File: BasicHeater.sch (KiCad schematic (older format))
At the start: 9 parts, among them J13 Thermistor

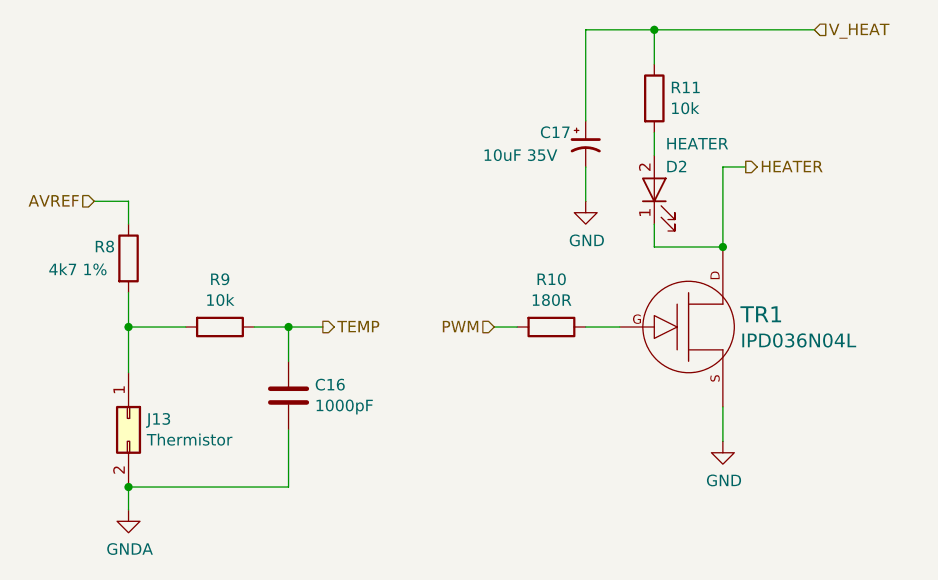
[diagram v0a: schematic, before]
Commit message: Assigned footprints for all components. Inductors are approximate size. MOSFETs dont agree with the footprints. Saved pcb netlist report as report.txt.
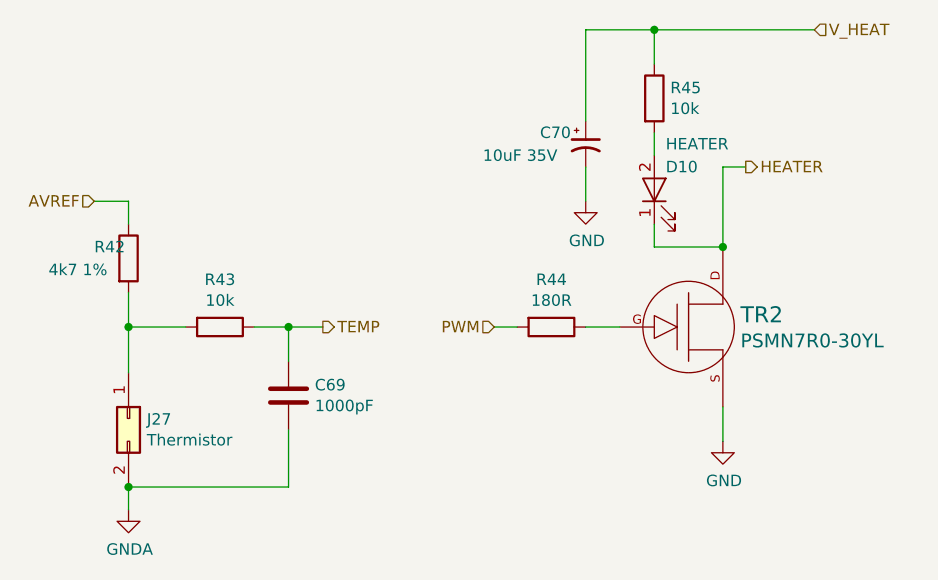
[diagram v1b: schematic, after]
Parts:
- C16: footprint (none) -> Capacitor_SMD:C_0603_1608Metric
- C17: footprint (none) -> Capacitor_SMD:CP_Elec_4x5.3
- D2: footprint (none) -> LED_SMD:LED_0603_1608Metric
- J13: footprint (none) -> Connector_PinHeader_2.54mm:PinHeader_1x02_P2.54mm_Vertical
- R10, R11, R8, R9: footprint (none) -> Resistor_SMD:R_0603_1608Metric
- TR1: value IPD036N04L -> PSMN7R0-30YL; footprint (none) -> Package_TO_SOT_SMD:SOT-669_LFPAK
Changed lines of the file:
@@
 AR Path="/5AC337B6/5AD9F95A/5AD4D269/5AD4D3D5" Ref="J27"  Part="1"
 AR Path="/5AB8F10D/5AD4D3D5" Ref="J28"  Part="1"
-F 0 "J13" V 2954 3730 50  0000 L CNN
+F 0 "J27" V 2954 3730 50  0000 L CNN
 F 1 "Thermistor" V 3045 3730 50  0000 L CNN
-F 2 "" H 2950 3650 50  0001 C CNN
+F 2 "Connector_PinHeader_2.54mm:PinHeader_1x02_P2.54mm_Vertical" H 2950 3650 50  0001 C CNN
 F 3 "~" H 2950 3650 50  0001 C CNN
 	1    2950 3650
@@
 AR Path="/5AC337B6/5AD9F95A/5AD4D269/5AD4D4AD" Ref="R42"  Part="1"
 AR Path="/5AB8F10D/5AD4D4AD" Ref="R46"  Part="1"
-F 0 "R8" H 2800 3000 50  0000 L CNN
+F 0 "R42" H 2800 3000 50  0000 L CNN
 F 1 "4k7 1%" H 2600 2900 50  0000 L CNN
-F 2 "" V 2880 2950 50  0001 C CNN
+F 2 "Resistor_SMD:R_0603_1608Metric" V 2880 2950 50  0001 C CNN
 F 3 "~" H 2950 2950 50  0001 C CNN
 	1    2950 2950
@@
 AR Path="/5AC337B6/5AD9F95A/5AD4D269/5AD4D50F" Ref="R43"  Part="1"
 AR Path="/5AB8F10D/5AD4D50F" Ref="R47"  Part="1"
-F 0 "R9" V 3143 3250 50  0000 C CNN
+F 0 "R43" V 3143 3250 50  0000 C CNN
 F 1 "10k" V 3234 3250 50  0000 C CNN
-F 2 "" V 3280 3250 50  0001 C CNN
+F 2 "Resistor_SMD:R_0603_1608Metric" V 3280 3250 50  0001 C CNN
 F 3 "~" H 3350 3250 50  0001 C CNN
 	1    3350 3250
@@
 AR Path="/5AC337B6/5AD9F95A/5AD4D269/5AD4D569" Ref="C69"  Part="1"
 AR Path="/5AB8F10D/5AD4D569" Ref="C71"  Part="1"
-F 0 "C16" H 3765 3596 50  0000 L CNN
+F 0 "C69" H 3765 3596 50  0000 L CNN
 F 1 "1000pF" H 3765 3505 50  0000 L CNN
-F 2 "" H 3688 3400 50  0001 C CNN
+F 2 "Capacitor_SMD:C_0603_1608Metric" H 3688 3400 50  0001 C CNN
 F 3 "~" H 3650 3550 50  0001 C CNN
 	1    3650 3550
@@
 AR Path="/5AC337B6/5AD9F95A/5AD4D269/5AD4D990" Ref="R44"  Part="1"
 AR Path="/5AB8F10D/5AD4D990" Ref="R48"  Part="1"
-F 0 "R10" V 4593 3250 50  0000 C CNN
+F 0 "R44" V 4593 3250 50  0000 C CNN
 F 1 "180R" V 4684 3250 50  0000 C CNN
-F 2 "" V 4730 3250 50  0001 C CNN
+F 2 "Resistor_SMD:R_0603_1608Metric" V 4730 3250 50  0001 C CNN
 F 3 "~" H 4800 3250 50  0001 C CNN
 	1    4800 3250
@@
 AR Path="/5AC337B6/5AD9F95A/5AD4D269/5AD51003" Ref="TR2"  Part="1"
 AR Path="/5AB8F10D/5AD51003" Ref="TR3"  Part="1"
-F 0 "TR1" H 5627 3303 70  0000 L CNN
-F 1 "IPD036N04L" H 5627 3189 60  0000 L CNN
-F 2 "" H 5400 3250 60  0000 C CNN
+F 0 "TR2" H 5627 3303 70  0000 L CNN
+F 1 "PSMN7R0-30YL" H 5627 3189 60  0000 L CNN
+F 2 "Package_TO_SOT_SMD:SOT-669_LFPAK" H 5400 3250 60  0001 C CNN
 F 3 "" H 5400 3250 60  0000 C CNN
 	1    5400 3250
@@
 AR Path="/5AC337B6/5AD9F95A/5AD4D269/5AD51206" Ref="C70"  Part="1"
 AR Path="/5AB8F10D/5AD51206" Ref="C72"  Part="1"
-F 0 "C17" H 4750 2500 50  0000 L CNN
+F 0 "C70" H 4750 2500 50  0000 L CNN
 F 1 "10uF 35V" H 4500 2400 50  0000 L CNN
-F 2 "" H 4950 2450 50  0001 C CNN
+F 2 "Capacitor_SMD:CP_Elec_4x5.3" H 4950 2450 50  0001 C CNN
 F 3 "~" H 4950 2450 50  0001 C CNN
 	1    4950 2450
@@
 AR Path="/5AC337B6/5AD9F95A/5AD4D269/5AD512CE" Ref="R45"  Part="1"
 AR Path="/5AB8F10D/5AD512CE" Ref="R49"  Part="1"
-F 0 "R11" H 5320 2296 50  0000 L CNN
+F 0 "R45" H 5320 2296 50  0000 L CNN
 F 1 "10k" H 5320 2205 50  0000 L CNN
-F 2 "" V 5180 2250 50  0001 C CNN
+F 2 "Resistor_SMD:R_0603_1608Metric" V 5180 2250 50  0001 C CNN
 F 3 "~" H 5250 2250 50  0001 C CNN
 	1    5250 2250
@@
 AR Path="/5AC337B6/5AD9F95A/5AD4D269/5AD513CB" Ref="D10"  Part="1"
 AR Path="/5AB8F10D/5AD513CB" Ref="D11"  Part="1"
-F 0 "D2" V 5350 2600 50  0000 R CNN
+F 0 "D10" V 5350 2600 50  0000 R CNN
 F 1 "HEATER" V 5450 2600 50  0000 R CNN
-F 2 "" H 5250 2650 50  0001 C CNN
+F 2 "LED_SMD:LED_0603_1608Metric" H 5250 2650 50  0001 C CNN
 F 3 "~" H 5250 2650 50  0001 C CNN
 	1    5250 2650

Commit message: Updated components. Removed power supply. Component layout on PCB.
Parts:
- TR1: footprint Package_TO_SOT_SMD:SOT-669_LFPAK -> PrntrBoardV1:SOT-669_LFPAK
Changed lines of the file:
@@
 $Descr A4 11693 8268
 encoding utf-8
-Sheet 7 35
+Sheet 7 34
 Title ""
 Date ""
@@
 $Comp
 L Connector_Generic:Conn_02x01 J13
-U 1 1 5AD4D3D5
+U 1 1 5ACEEAAB
 P 2950 3650
-AR Path="/5AC337B6/5ACBE919/5AD4D269/5AD4D3D5" Ref="J13"  Part="1"
-AR Path="/5AC337B6/5AD9F95A/5AD4D269/5AD4D3D5" Ref="J27"  Part="1"
-AR Path="/5AB8F10D/5AD4D3D5" Ref="J28"  Part="1"
+AR Path="/5AC337B6/5ACBE919/5AD4D269/5ACEEAAB" Ref="J13"  Part="1"
+AR Path="/5AC337B6/5AD9F95A/5AD4D269/5ACEEAAB" Ref="J27"  Part="1"
+AR Path="/5AB8F10D/5ACEEAAB" Ref="J28"  Part="1"
 F 0 "J27" V 2954 3730 50  0000 L CNN
 F 1 "Thermistor" V 3045 3730 50  0000 L CNN
@@
 $Comp
 L power:GNDA #PWR020
-U 1 1 5AD4D481
+U 1 1 5ACEEAAC
 P 2950 4050
-AR Path="/5AC337B6/5ACBE919/5AD4D269/5AD4D481" Ref="#PWR020"  Part="1"
-AR Path="/5AC337B6/5AD9F95A/5AD4D269/5AD4D481" Ref="#PWR065"  Part="1"
-AR Path="/5AB8F10D/5AD4D481" Ref="#PWR068"  Part="1"
+AR Path="/5AC337B6/5ACBE919/5AD4D269/5ACEEAAC" Ref="#PWR020"  Part="1"
+AR Path="/5AC337B6/5AD9F95A/5AD4D269/5ACEEAAC" Ref="#PWR065"  Part="1"
+AR Path="/5AB8F10D/5ACEEAAC" Ref="#PWR068"  Part="1"
 F 0 "#PWR065" H 2950 3800 50  0001 C CNN
 F 1 "GNDA" H 2955 3877 50  0000 C CNN
@@
 $Comp
 L Device:R R8
-U 1 1 5AD4D4AD
+U 1 1 5ACEEAAD
 P 2950 2950
-AR Path="/5AC337B6/5ACBE919/5AD4D269/5AD4D4AD" Ref="R8"  Part="1"
-AR Path="/5AC337B6/5AD9F95A/5AD4D269/5AD4D4AD" Ref="R42"  Part="1"
-AR Path="/5AB8F10D/5AD4D4AD" Ref="R46"  Part="1"
+AR Path="/5AC337B6/5ACBE919/5AD4D269/5ACEEAAD" Ref="R8"  Part="1"
+AR Path="/5AC337B6/5AD9F95A/5AD4D269/5ACEEAAD" Ref="R42"  Part="1"
+AR Path="/5AB8F10D/5ACEEAAD" Ref="R46"  Part="1"
 F 0 "R42" H 2800 3000 50  0000 L CNN
 F 1 "4k7 1%" H 2600 2900 50  0000 L CNN
@@
 $Comp
 L Device:R R9
-U 1 1 5AD4D50F
+U 1 1 5ACEEAAE
 P 3350 3250
-AR Path="/5AC337B6/5ACBE919/5AD4D269/5AD4D50F" Ref="R9"  Part="1"
-AR Path="/5AC337B6/5AD9F95A/5AD4D269/5AD4D50F" Ref="R43"  Part="1"
-AR Path="/5AB8F10D/5AD4D50F" Ref="R47"  Part="1"
+AR Path="/5AC337B6/5ACBE919/5AD4D269/5ACEEAAE" Ref="R9"  Part="1"
+AR Path="/5AC337B6/5AD9F95A/5AD4D269/5ACEEAAE" Ref="R43"  Part="1"
+AR Path="/5AB8F10D/5ACEEAAE" Ref="R47"  Part="1"
 F 0 "R43" V 3143 3250 50  0000 C CNN
 F 1 "10k" V 3234 3250 50  0000 C CNN
@@
 $Comp
 L Device:R R10
-U 1 1 5AD4D990
+U 1 1 5ACEEAB0
 P 4800 3250
-AR Path="/5AC337B6/5ACBE919/5AD4D269/5AD4D990" Ref="R10"  Part="1"
-AR Path="/5AC337B6/5AD9F95A/5AD4D269/5AD4D990" Ref="R44"  Part="1"
-AR Path="/5AB8F10D/5AD4D990" Ref="R48"  Part="1"
+AR Path="/5AC337B6/5ACBE919/5AD4D269/5ACEEAB0" Ref="R10"  Part="1"
+AR Path="/5AC337B6/5AD9F95A/5AD4D269/5ACEEAB0" Ref="R44"  Part="1"
+AR Path="/5AB8F10D/5ACEEAB0" Ref="R48"  Part="1"
 F 0 "R44" V 4593 3250 50  0000 C CNN
 F 1 "180R" V 4684 3250 50  0000 C CNN
@@
 F 0 "TR2" H 5627 3303 70  0000 L CNN
 F 1 "PSMN7R0-30YL" H 5627 3189 60  0000 L CNN
-F 2 "Package_TO_SOT_SMD:SOT-669_LFPAK" H 5400 3250 60  0001 C CNN
+F 2 "PrntrBoardV1:SOT-669_LFPAK" H 5400 3250 60  0001 C CNN
 F 3 "" H 5400 3250 60  0000 C CNN
 	1    5400 3250
@@
 $Comp
 L Device:LED D2
-U 1 1 5AD513CB
+U 1 1 5ACEEAB5
 P 5250 2650
-AR Path="/5AC337B6/5ACBE919/5AD4D269/5AD513CB" Ref="D2"  Part="1"
-AR Path="/5AC337B6/5AD9F95A/5AD4D269/5AD513CB" Ref="D10"  Part="1"
-AR Path="/5AB8F10D/5AD513CB" Ref="D11"  Part="1"
+AR Path="/5AC337B6/5ACBE919/5AD4D269/5ACEEAB5" Ref="D2"  Part="1"
+AR Path="/5AC337B6/5AD9F95A/5AD4D269/5ACEEAB5" Ref="D10"  Part="1"
+AR Path="/5AB8F10D/5ACEEAB5" Ref="D11"  Part="1"
 F 0 "D10" V 5350 2600 50  0000 R CNN
 F 1 "HEATER" V 5450 2600 50  0000 R CNN
@@
 $Comp
 L power:GND #PWR021
-U 1 1 5AD515DD
+U 1 1 5ACEEAB6
 P 4950 2700
-AR Path="/5AC337B6/5ACBE919/5AD4D269/5AD515DD" Ref="#PWR021"  Part="1"
-AR Path="/5AC337B6/5AD9F95A/5AD4D269/5AD515DD" Ref="#PWR066"  Part="1"
-AR Path="/5AB8F10D/5AD515DD" Ref="#PWR069"  Part="1"
+AR Path="/5AC337B6/5ACBE919/5AD4D269/5ACEEAB6" Ref="#PWR021"  Part="1"
+AR Path="/5AC337B6/5AD9F95A/5AD4D269/5ACEEAB6" Ref="#PWR066"  Part="1"
+AR Path="/5AB8F10D/5ACEEAB6" Ref="#PWR069"  Part="1"
 F 0 "#PWR066" H 4950 2450 50  0001 C CNN
 F 1 "GND" H 4955 2527 50  0000 C CNN

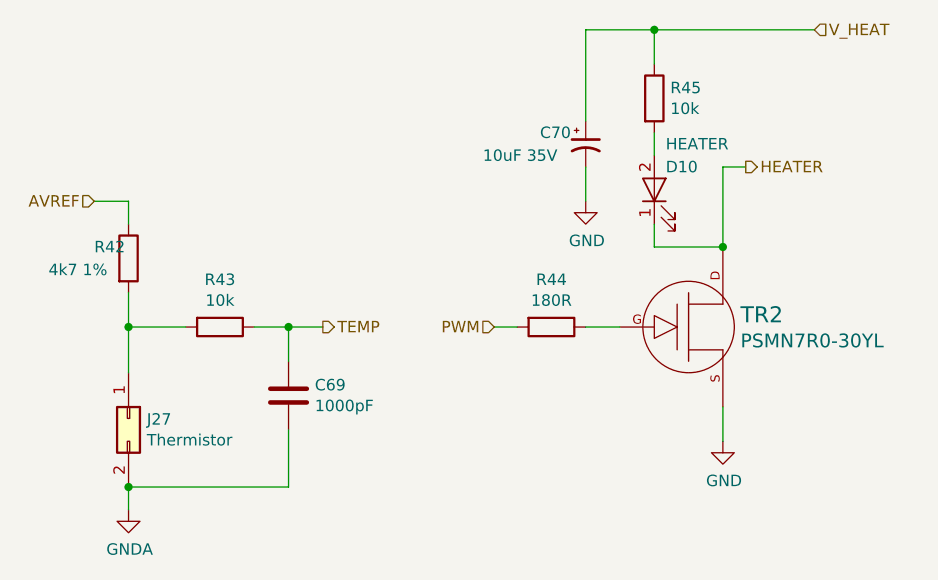
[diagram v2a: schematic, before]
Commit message: Routed most of the power traces.
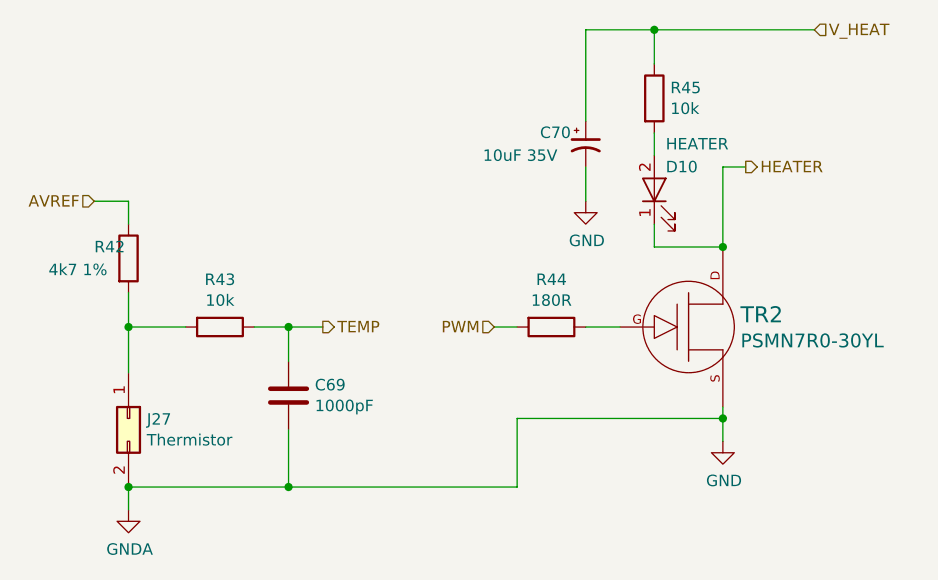
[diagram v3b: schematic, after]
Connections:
- net GNDA is gone; now on net GND: C16.2, J13.2 (Pin_2)
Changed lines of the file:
@@
 $Descr A4 11693 8268
 encoding utf-8
-Sheet 7 34
+Sheet 29 34
 Title ""
 Date ""
@@
 $EndComp
 Wire Wire Line
-	5550 3600 5550 3750
+	5550 3600 5550 3650
 $Comp
 L Device:CP1_Small C17
@@
 Wire Wire Line
 	5650 2550 5550 2550
+Wire Wire Line
+	3650 3950 4650 3950
+Wire Wire Line
+	4650 3950 4650 3650
+Connection ~ 3650 3950
+Wire Wire Line
+	4650 3650 5550 3650
+Connection ~ 5550 3650
+Wire Wire Line
+	5550 3650 5550 3750
 $EndSCHEMATC

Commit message: Added mounting holes and fiducials. Placed all components labels so they are readable.
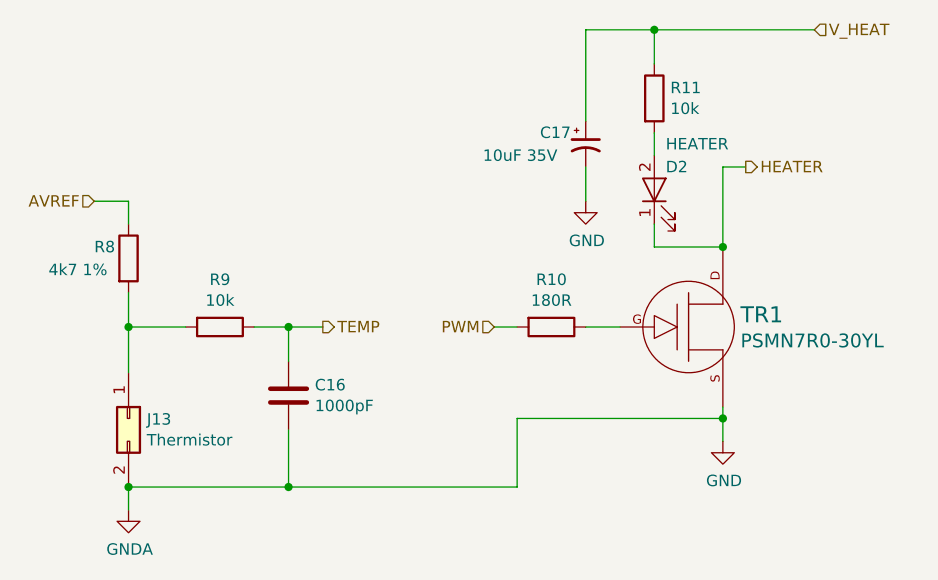
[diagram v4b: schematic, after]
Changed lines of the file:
@@
 AR Path="/5AC337B6/5AD9F95A/5AD4D269/5ACEEAAB" Ref="J27"  Part="1"
 AR Path="/5AB8F10D/5ACEEAAB" Ref="J28"  Part="1"
-F 0 "J27" V 2954 3730 50  0000 L CNN
+F 0 "J13" V 2954 3730 50  0000 L CNN
 F 1 "Thermistor" V 3045 3730 50  0000 L CNN
 F 2 "Connector_PinHeader_2.54mm:PinHeader_1x02_P2.54mm_Vertical" H 2950 3650 50  0001 C CNN
@@
 AR Path="/5AC337B6/5AD9F95A/5AD4D269/5ACEEAAD" Ref="R42"  Part="1"
 AR Path="/5AB8F10D/5ACEEAAD" Ref="R46"  Part="1"
-F 0 "R42" H 2800 3000 50  0000 L CNN
+F 0 "R8" H 2800 3000 50  0000 L CNN
 F 1 "4k7 1%" H 2600 2900 50  0000 L CNN
 F 2 "Resistor_SMD:R_0603_1608Metric" V 2880 2950 50  0001 C CNN
@@
 AR Path="/5AC337B6/5AD9F95A/5AD4D269/5ACEEAAE" Ref="R43"  Part="1"
 AR Path="/5AB8F10D/5ACEEAAE" Ref="R47"  Part="1"
-F 0 "R43" V 3143 3250 50  0000 C CNN
+F 0 "R9" V 3143 3250 50  0000 C CNN
 F 1 "10k" V 3234 3250 50  0000 C CNN
 F 2 "Resistor_SMD:R_0603_1608Metric" V 3280 3250 50  0001 C CNN
@@
 AR Path="/5AC337B6/5AD9F95A/5AD4D269/5AD4D569" Ref="C69"  Part="1"
 AR Path="/5AB8F10D/5AD4D569" Ref="C71"  Part="1"
-F 0 "C69" H 3765 3596 50  0000 L CNN
+F 0 "C16" H 3765 3596 50  0000 L CNN
 F 1 "1000pF" H 3765 3505 50  0000 L CNN
 F 2 "Capacitor_SMD:C_0603_1608Metric" H 3688 3400 50  0001 C CNN
@@
 AR Path="/5AC337B6/5AD9F95A/5AD4D269/5ACEEAB0" Ref="R44"  Part="1"
 AR Path="/5AB8F10D/5ACEEAB0" Ref="R48"  Part="1"
-F 0 "R44" V 4593 3250 50  0000 C CNN
+F 0 "R10" V 4593 3250 50  0000 C CNN
 F 1 "180R" V 4684 3250 50  0000 C CNN
 F 2 "Resistor_SMD:R_0603_1608Metric" V 4730 3250 50  0001 C CNN
@@
 AR Path="/5AC337B6/5AD9F95A/5AD4D269/5AD51003" Ref="TR2"  Part="1"
 AR Path="/5AB8F10D/5AD51003" Ref="TR3"  Part="1"
-F 0 "TR2" H 5627 3303 70  0000 L CNN
+F 0 "TR1" H 5627 3303 70  0000 L CNN
 F 1 "PSMN7R0-30YL" H 5627 3189 60  0000 L CNN
 F 2 "PrntrBoardV1:SOT-669_LFPAK" H 5400 3250 60  0001 C CNN
@@
 AR Path="/5AC337B6/5AD9F95A/5AD4D269/5AD51206" Ref="C70"  Part="1"
 AR Path="/5AB8F10D/5AD51206" Ref="C72"  Part="1"
-F 0 "C70" H 4750 2500 50  0000 L CNN
+F 0 "C17" H 4750 2500 50  0000 L CNN
 F 1 "10uF 35V" H 4500 2400 50  0000 L CNN
 F 2 "Capacitor_SMD:CP_Elec_4x5.3" H 4950 2450 50  0001 C CNN
@@
 AR Path="/5AC337B6/5AD9F95A/5AD4D269/5AD512CE" Ref="R45"  Part="1"
 AR Path="/5AB8F10D/5AD512CE" Ref="R49"  Part="1"
-F 0 "R45" H 5320 2296 50  0000 L CNN
+F 0 "R11" H 5320 2296 50  0000 L CNN
 F 1 "10k" H 5320 2205 50  0000 L CNN
 F 2 "Resistor_SMD:R_0603_1608Metric" V 5180 2250 50  0001 C CNN
@@
 AR Path="/5AC337B6/5AD9F95A/5AD4D269/5ACEEAB5" Ref="D10"  Part="1"
 AR Path="/5AB8F10D/5ACEEAB5" Ref="D11"  Part="1"
-F 0 "D10" V 5350 2600 50  0000 R CNN
+F 0 "D2" V 5350 2600 50  0000 R CNN
 F 1 "HEATER" V 5450 2600 50  0000 R CNN
 F 2 "LED_SMD:LED_0603_1608Metric" H 5250 2650 50  0001 C CNN

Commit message: Update schematics to use TMC5130/TMC2130 drivers.
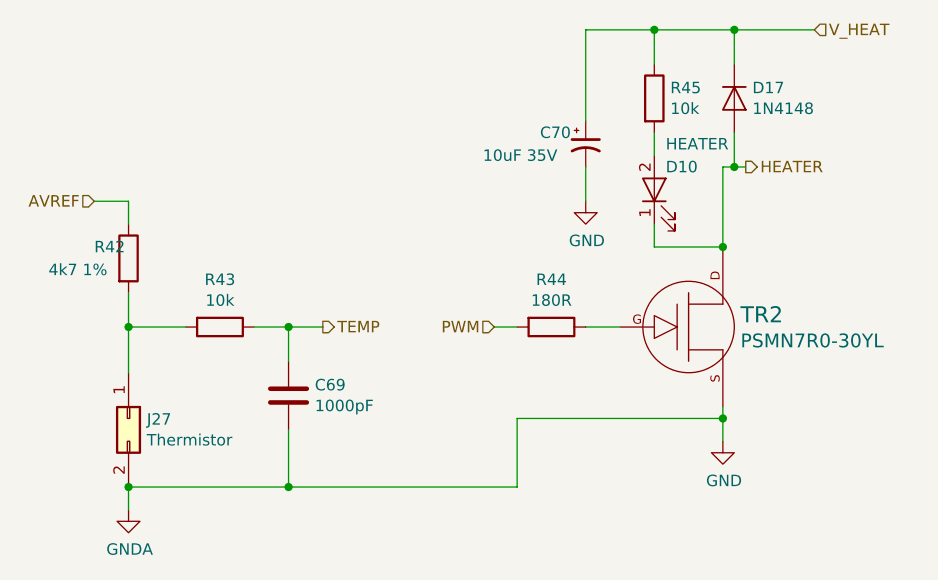
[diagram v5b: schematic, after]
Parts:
- added D17: 1N4148, Diode_SMD:D_SOD-323F, symbol Device:D
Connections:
- net HEATER: now also D17.2 (A)
- net V_HEAT: now also D17.1 (K)
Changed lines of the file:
@@
 AR Path="/5AC337B6/5AD9F95A/5AD4D269/5ACEEAAB" Ref="J27"  Part="1"
 AR Path="/5AB8F10D/5ACEEAAB" Ref="J28"  Part="1"
-F 0 "J13" V 2954 3730 50  0000 L CNN
+F 0 "J27" V 2954 3730 50  0000 L CNN
 F 1 "Thermistor" V 3045 3730 50  0000 L CNN
 F 2 "Connector_PinHeader_2.54mm:PinHeader_1x02_P2.54mm_Vertical" H 2950 3650 50  0001 C CNN
@@
 AR Path="/5AC337B6/5AD9F95A/5AD4D269/5ACEEAAD" Ref="R42"  Part="1"
 AR Path="/5AB8F10D/5ACEEAAD" Ref="R46"  Part="1"
-F 0 "R8" H 2800 3000 50  0000 L CNN
+F 0 "R42" H 2800 3000 50  0000 L CNN
 F 1 "4k7 1%" H 2600 2900 50  0000 L CNN
 F 2 "Resistor_SMD:R_0603_1608Metric" V 2880 2950 50  0001 C CNN
@@
 AR Path="/5AC337B6/5AD9F95A/5AD4D269/5ACEEAAE" Ref="R43"  Part="1"
 AR Path="/5AB8F10D/5ACEEAAE" Ref="R47"  Part="1"
-F 0 "R9" V 3143 3250 50  0000 C CNN
+F 0 "R43" V 3143 3250 50  0000 C CNN
 F 1 "10k" V 3234 3250 50  0000 C CNN
 F 2 "Resistor_SMD:R_0603_1608Metric" V 3280 3250 50  0001 C CNN
@@
 AR Path="/5AC337B6/5AD9F95A/5AD4D269/5AD4D569" Ref="C69"  Part="1"
 AR Path="/5AB8F10D/5AD4D569" Ref="C71"  Part="1"
-F 0 "C16" H 3765 3596 50  0000 L CNN
+F 0 "C69" H 3765 3596 50  0000 L CNN
 F 1 "1000pF" H 3765 3505 50  0000 L CNN
 F 2 "Capacitor_SMD:C_0603_1608Metric" H 3688 3400 50  0001 C CNN
@@
 AR Path="/5AC337B6/5AD9F95A/5AD4D269/5ACEEAB0" Ref="R44"  Part="1"
 AR Path="/5AB8F10D/5ACEEAB0" Ref="R48"  Part="1"
-F 0 "R10" V 4593 3250 50  0000 C CNN
+F 0 "R44" V 4593 3250 50  0000 C CNN
 F 1 "180R" V 4684 3250 50  0000 C CNN
 F 2 "Resistor_SMD:R_0603_1608Metric" V 4730 3250 50  0001 C CNN
@@
 AR Path="/5AC337B6/5AD9F95A/5AD4D269/5AD51003" Ref="TR2"  Part="1"
 AR Path="/5AB8F10D/5AD51003" Ref="TR3"  Part="1"
-F 0 "TR1" H 5627 3303 70  0000 L CNN
+F 0 "TR2" H 5627 3303 70  0000 L CNN
 F 1 "PSMN7R0-30YL" H 5627 3189 60  0000 L CNN
 F 2 "PrntrBoardV1:SOT-669_LFPAK" H 5400 3250 60  0001 C CNN
@@
 AR Path="/5AC337B6/5AD9F95A/5AD4D269/5AD51206" Ref="C70"  Part="1"
 AR Path="/5AB8F10D/5AD51206" Ref="C72"  Part="1"
-F 0 "C17" H 4750 2500 50  0000 L CNN
+F 0 "C70" H 4750 2500 50  0000 L CNN
 F 1 "10uF 35V" H 4500 2400 50  0000 L CNN
 F 2 "Capacitor_SMD:CP_Elec_4x5.3" H 4950 2450 50  0001 C CNN
@@
 AR Path="/5AC337B6/5AD9F95A/5AD4D269/5AD512CE" Ref="R45"  Part="1"
 AR Path="/5AB8F10D/5AD512CE" Ref="R49"  Part="1"
-F 0 "R11" H 5320 2296 50  0000 L CNN
+F 0 "R45" H 5320 2296 50  0000 L CNN
 F 1 "10k" H 5320 2205 50  0000 L CNN
 F 2 "Resistor_SMD:R_0603_1608Metric" V 5180 2250 50  0001 C CNN
@@
 AR Path="/5AC337B6/5AD9F95A/5AD4D269/5ACEEAB5" Ref="D10"  Part="1"
 AR Path="/5AB8F10D/5ACEEAB5" Ref="D11"  Part="1"
-F 0 "D2" V 5350 2600 50  0000 R CNN
+F 0 "D10" V 5350 2600 50  0000 R CNN
 F 1 "HEATER" V 5450 2600 50  0000 R CNN
 F 2 "LED_SMD:LED_0603_1608Metric" H 5250 2650 50  0001 C CNN
@@
 Connection ~ 5250 1950
 Wire Wire Line
-	5250 1950 5950 1950
+	5250 1950 5600 1950
 Wire Wire Line
 	5250 2400 5250 2500
@@
 HEATER
 Wire Wire Line
-	5650 2550 5550 2550
+	5650 2550 5600 2550
 Wire Wire Line
 	3650 3950 4650 3950
@@
 Wire Wire Line
 	5550 3650 5550 3750
+$Comp
+L Device:D D17
+U 1 1 5ACF27DC
+P 5600 2250
+AR Path="/5AC337B6/5AD9F95A/5AD4D269/5ACF27DC" Ref="D17"  Part="1"
+AR Path="/5AC337B6/5ACBE919/5AD4D269/5ACF27DC" Ref="D16"  Part="1"
+F 0 "D17" V 5554 2329 50  0000 L CNN
+F 1 "1N4148" V 5645 2329 50  0000 L CNN
+F 2 "Diode_SMD:D_SOD-323F" H 5600 2250 50  0001 C CNN
+F 3 "~" H 5600 2250 50  0001 C CNN
+	1    5600 2250
+	0    1    1    0
+$EndComp
+Wire Wire Line
+	5600 2100 5600 1950
+Connection ~ 5600 1950
+Wire Wire Line
+	5600 1950 5950 1950
+Wire Wire Line
+	5600 2400 5600 2550
+Connection ~ 5600 2550
+Wire Wire Line
+	5600 2550 5550 2550
 $EndSCHEMATC

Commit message: Switched to local foorprints for terminals and LED. Switched to local foorprint for the printer driver ship - it has larger thermal pad ares.
Placement V1 complete.
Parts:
- D2: footprint LED_SMD:LED_0603_1608Metric -> PrntrBoardV1:LED_0603_1608Metric
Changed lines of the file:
@@
 F 0 "D10" V 5350 2600 50  0000 R CNN
 F 1 "HEATER" V 5450 2600 50  0000 R CNN
-F 2 "LED_SMD:LED_0603_1608Metric" H 5250 2650 50  0001 C CNN
+F 2 "PrntrBoardV1:LED_0603_1608Metric" H 5250 2650 50  0001 C CNN
 F 3 "~" H 5250 2650 50  0001 C CNN
 	1    5250 2650
